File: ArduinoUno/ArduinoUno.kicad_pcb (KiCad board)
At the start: 2 copper layers, 4 parts, among them U1 LM358D, U2 LM358D, U3 LM358D, U4 LM358D

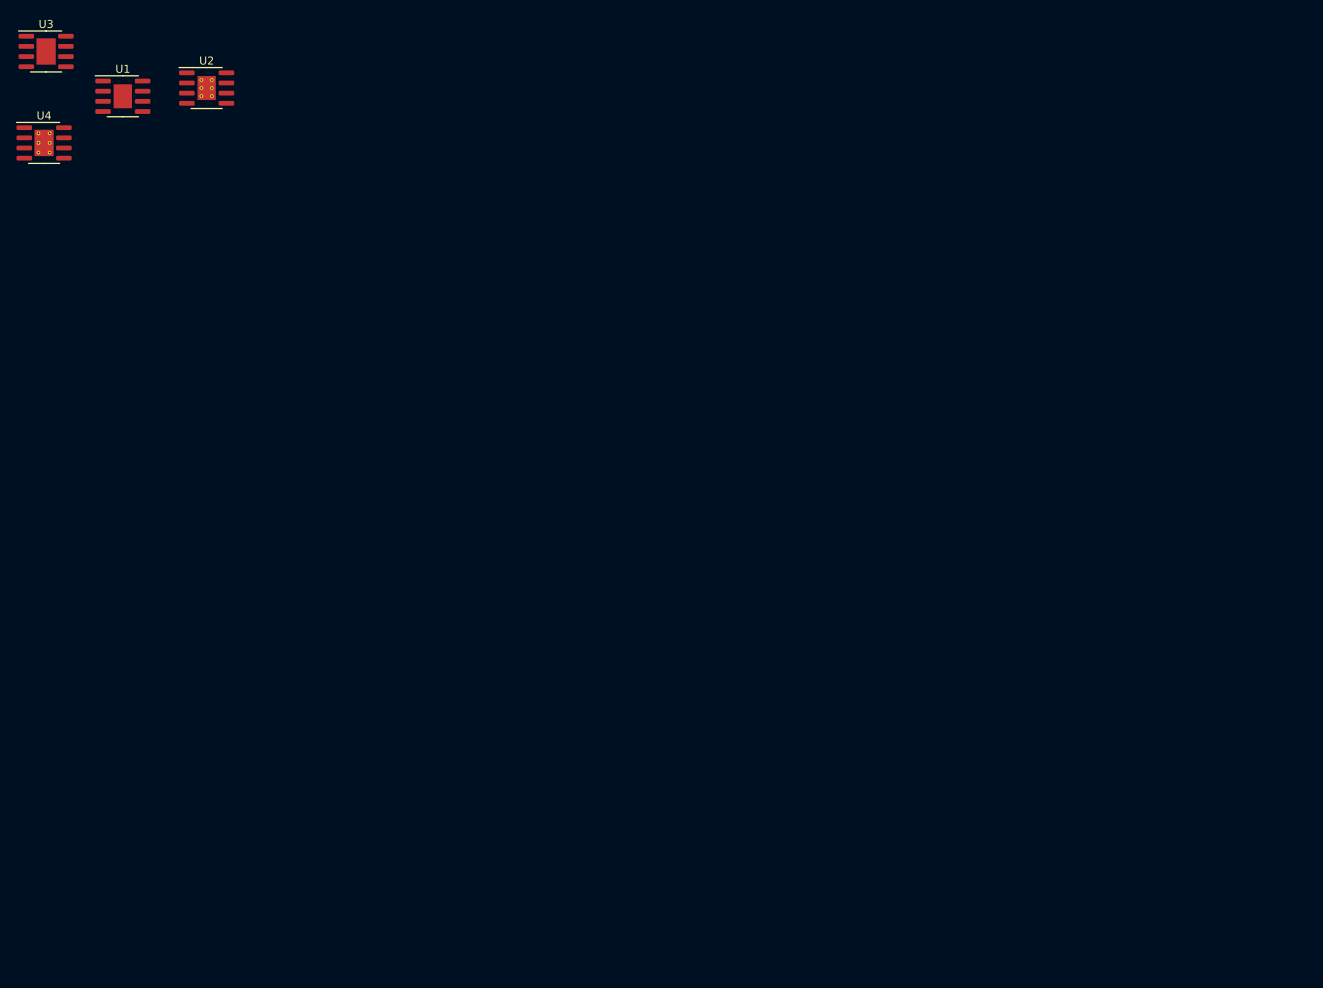
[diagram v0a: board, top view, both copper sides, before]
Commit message: Arduino CH340
Change footprint, 3D model etc
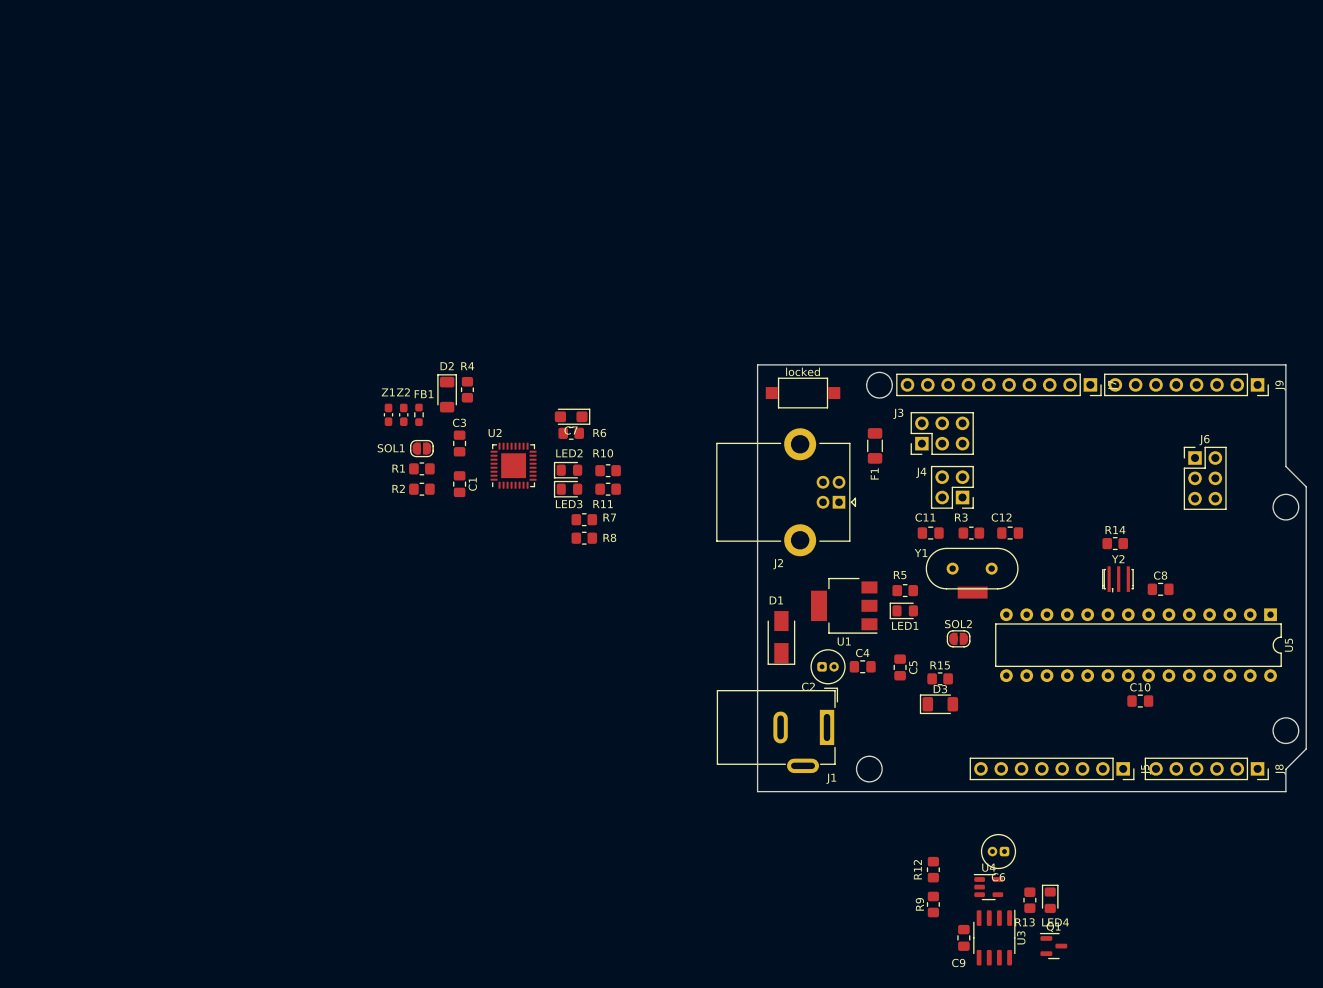
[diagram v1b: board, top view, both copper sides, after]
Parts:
- added C1: 100nF, 02pyzPassive:C_0805_HandSolder, F.Cu at (92.1, 82.8)
- added C10: 100nF, 02pyzPassive:C_0805_HandSolder, F.Cu at (177.2, 109.9)
- added C11: 100nF, 02pyzPassive:C_0805_HandSolder, F.Cu at (151.0, 88.9)
- added C12: 100nF, 02pyzPassive:C_0805_HandSolder, F.Cu at (160.9, 88.9)
- added C2: 47uF, 02pyzPassive:C_Radial_D4.0mm_H5.0mm_P1.50mm, F.Cu at (137.4, 105.6)
- added C3: 22pF, 02pyzPassive:C_0805_HandSolder, F.Cu at (92.1, 77.7)
- added C4: 22pF, 02pyzPassive:C_0805_HandSolder, F.Cu at (142.5, 105.6)
- added C5: 100nF, 02pyzPassive:C_0805_HandSolder, F.Cu at (147.1, 105.7)
- added C6: 47uF, 02pyzPassive:C_Radial_D4.0mm_H5.0mm_P1.50mm, F.Cu at (160.2, 128.7)
- added C7: 100nF, 02pyzPassive:CP_EIA-3216-10_Kemet-I, F.Cu at (106.0, 74.4)
- added C8: 100nF, 02pyzPassive:C_0805_HandSolder, F.Cu at (179.7, 95.9)
- added C9: 100nF, 02pyzPassive:C_0805_HandSolder, F.Cu at (155.1, 139.5)
- added D1: D, 03pyzActive:D_SMA, F.Cu at (132.3, 101.9)
- added D2: CD1206-S01575, 03pyzActive:D_1206_HandSolder, F.Cu at (90.5, 71.6)
- added D3: CD1206-S01575, 03pyzActive:D_1206_HandSolder, F.Cu at (152.2, 110.3)
- added F1: Fuse, 02pyzPassive:C_1206_HandSolder, F.Cu at (144.0, 78.0)
- added FB1: BLM21PG221SN1D, 02pyzPassive:R_0603_HandSolder, F.Cu at (87.0, 74.1)
- added H1: MountingHole, 01pyzGeneral:MountingHole_3.2mm_M3, F.Cu at (144.6, 70.4)
- added H2: MountingHole, 01pyzGeneral:MountingHole_3.2mm_M3, F.Cu at (143.3, 118.4)
- added H3: MountingHole, 01pyzGeneral:MountingHole_3.2mm_M3, F.Cu at (195.4, 85.7)
- added H4: MountingHole, 01pyzGeneral:MountingHole_3.2mm_M3, F.Cu at (195.4, 113.6)
- added J1: Jack_DC, 04pyzConnector:JackDC_Input_3.5mm, F.Cu at (138.0, 113.2)
- added J2: USB_B, 04pyzConnector:USB_B_Lumberg_2411_02_Horizontal, F.Cu at (139.5, 85.0)
- added J3: ICSP, 04pyzConnector:PinHeader_2x03_P2.54mm_Vertical, F.Cu at (149.9, 77.7)
- added J4: Conn_02x02, 04pyzConnector:PinHeader_2x02_P2.54mm_Vertical, F.Cu at (154.9, 84.5)
- added J5: POWER, 04pyzConnector:PinSocket_1x08_P2.54mm_Vertical, F.Cu at (175.0, 118.4)
- added J6: ICSPx, 04pyzConnector:PinHeader_2x03_P2.54mm_Vertical, F.Cu at (184.0, 79.5)
- added J7: DIG_PWM_8-13, 04pyzConnector:PinSocket_1x10_P2.54mm_Vertical, F.Cu at (170.9, 70.4)
- added J8: ANALOG, 04pyzConnector:PinSocket_1x06_P2.54mm_Vertical, F.Cu at (191.8, 118.4)
- added J9: DIG_PWM_0-7, 04pyzConnector:PinSocket_1x08_P2.54mm_Vertical, F.Cu at (191.8, 70.4)
- added LED1: LRED, 03pyzActive:D_0805_HandSolder, F.Cu at (147.8, 98.6)
- added LED2: TX, 03pyzActive:D_0805_HandSolder, F.Cu at (105.8, 81.0)
- added LED3: RX, 03pyzActive:D_0805_HandSolder, F.Cu at (105.8, 83.4)
- added LED4: LYELLOW, 03pyzActive:D_0805_HandSolder, F.Cu at (165.9, 134.8)
- added Q1: MOS-P_FDN304P, 03pyzActive:SOT-23, F.Cu at (166.4, 140.5)
- added R1: 22R, 02pyzPassive:R_0805_HandSolder, F.Cu at (87.4, 80.9)
- added R10: 1K, 02pyzPassive:R_0805_HandSolder, F.Cu at (110.6, 81.1)
- added R11: 1K, 02pyzPassive:R_0805_HandSolder, F.Cu at (110.6, 83.4)
- added R12: 10K, 02pyzPassive:R_0805_HandSolder, F.Cu at (151.3, 131.0)
- added R13: 470, 02pyzPassive:R_0805_HandSolder, F.Cu at (163.4, 134.8)
- added R14: 1M, 02pyzPassive:R_0805_HandSolder, F.Cu at (174.0, 90.2)
- added R15: 10K, 02pyzPassive:R_0805_HandSolder, F.Cu at (152.1, 107.1)
- added R2: 22R, 02pyzPassive:R_0805_HandSolder, F.Cu at (87.4, 83.4)
- added R3: 1M, 02pyzPassive:R_0805_HandSolder, F.Cu at (156.0, 88.9)
- added R4: 10K, 02pyzPassive:R_0805_HandSolder, F.Cu at (93.1, 71.0)
- added R5: 470, 02pyzPassive:R_0805_HandSolder, F.Cu at (147.8, 96.1)
- added R6: 1K, 02pyzPassive:R_0805_HandSolder, F.Cu at (106.0, 76.4)
- added R7: 1K, 02pyzPassive:R_0805_HandSolder, F.Cu at (107.7, 87.2)
- added R8: 1K, 02pyzPassive:R_0805_HandSolder, F.Cu at (107.7, 89.5)
- added R9: 10K, 02pyzPassive:R_0805_HandSolder, F.Cu at (151.3, 135.3)
- added SOL1: ~, 01pyzGeneral:SolderJumper-2_P1.3mm_Open_RoundedPad1.0x1.5mm, F.Cu at (87.4, 78.3)
- added SOL2: RESET_EN, 01pyzGeneral:SolderJumper-2_P1.3mm_Open_RoundedPad1.0x1.5mm, F.Cu at (154.4, 102.1)
- added U5: ATmega328-P, Package_DIP:DIP-28_W7.62mm, F.Cu at (193.4, 99.1)
- added Y1: 16MHz, 02pyzPassive:Crystal_HC49-4H_Vertical_GND, F.Cu at (153.7, 93.3)
- added Y2: 16MHz, 02pyzPassive:Resonator_SMD_Murata_CSTxExxV-3Pin_3.0x1.1mm_HandSoldering, F.Cu at (174.5, 94.7)
- added Z1: PGB1010604, 02pyzPassive:C_0603_HandSolder, F.Cu at (83.2, 74.1)
- added Z2: PGB1010604, 02pyzPassive:C_0603_HandSolder, F.Cu at (85.1, 74.1)
- added locked: SW_Push_NO, 06pyzSwitchRelay:SW_SPST_CK_RS282G05A3, F.Cu at (135.0, 71.4)
- U1: value LM358D -> MC33269-SOT; footprint 0pyzIC_MCU:SOIC-8-1EP_3.9x4.9mm_P1.27mm_EP2.29x3mm -> 07pyzIC_MCU:SOT-223
- U2: value LM358D -> ATmega16U2-M; footprint 0pyzIC_MCU:SOIC-8-1EP_3.9x4.9mm_P1.27mm_EP2.29x3mm_ThermalVias -> Package_DFN_QFN:QFN-32-1EP_5x5mm_P0.5mm_EP3.1x3.1mm
- U3: footprint 0pyzIC_MCU:SOIC-8-1EP_3.9x4.9mm_P1.27mm_EP2.41x3.3mm -> 07pyzIC_MCU:SOIC-8_3.9x4.9mm_P1.27mm
- U4: value LM358D -> LP2985-3.3; footprint 0pyzIC_MCU:SOIC-8-1EP_3.9x4.9mm_P1.27mm_EP2.41x3.3mm_ThermalVias -> Package_TO_SOT_SMD:SOT-23-5
- moved U3 162.3 mm to (158.9, 139.5), turned to -90 degrees
- moved U4 150.3 mm to (158.2, 133.2)
- moved U1 110.4 mm to (140.2, 98.0), turned to 180 degrees
- moved U2 60.8 mm to (98.8, 80.5), turned to 90 degrees
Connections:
- U1 pad 1: unconnected-(U1-OUTA-Pad1) -> GND
- U1 pad 2: unconnected-(U1-INPA--Pad2) -> +5V
- U1 pad 3: unconnected-(U1-INPA+-Pad3) -> VIN
- U1 pad 4: unconnected-(U1-V--Pad4) -> +5V
- U2 pad 1: unconnected-(U2-OUTA-Pad1) -> Net-(U2-XTAL1)
- U2 pad 2: unconnected-(U2-INPA--Pad2) -> Net-(U2-PC0/XTAL2)
- U2 pad 3: unconnected-(U2-INPA+-Pad3) -> GND
- U2 pad 4: unconnected-(U2-V--Pad4) -> +5V
- U2 pad 8: unconnected-(U2-V+-Pad8) -> Net-(U2-(AIN1/RXD1/INT2)PD2)
- U2 pad 9: (no net) -> Net-(U2-(TXD1/INT3)PD3)
- U3 pad 1: unconnected-(U3-OUTA-Pad1) -> Net-(Q1-G)
- U3 pad 2: unconnected-(U3-INPA--Pad2) -> +3V3
- U3 pad 3: unconnected-(U3-INPA+-Pad3) -> Net-(U3-INPA+)
- U3 pad 4: unconnected-(U3-V--Pad4) -> GND
- U3 pad 5: unconnected-(U3-INPB--Pad5) -> /ICSP_SCLK
- U3 pad 6: unconnected-(U3-INPB+-Pad6) -> Net-(U3-INPB+)
- U3 pad 7: unconnected-(U3-OUTB-Pad7) -> Net-(U3-INPB+)
- U3 pad 8: unconnected-(U3-V+-Pad8) -> +5V
- U4 pad 1: unconnected-(U4-OUTA-Pad1) -> +5V
- U4 pad 2: unconnected-(U4-INPA--Pad2) -> GND
- U4 pad 3: unconnected-(U4-INPA+-Pad3) -> +5V
- U4 pad 5: unconnected-(U4-INPB--Pad5) -> +3V3
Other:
- board outline added: 68.6 x 53.3 mm
